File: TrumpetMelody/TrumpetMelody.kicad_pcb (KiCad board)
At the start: 2 copper layers, 76.2 x 68.6 mm, 79 parts, among them J1 USB_B_Micro, J2 Conn_01x05, J3 640456-3, J4 640456-3, SW1 SW_Push, U1 STM32F411RETx, U2 TLV62565DBVR, U3 MAX98357AETE_T, U4 MAX7375AXR805

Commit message: Placed vias so we can connect USB_ID and USB_VSENSE later if needed
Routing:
- net USB_VSENSE: track 2.18 -> 28.8 mm
- net USB_ID: track 2.79 -> 27.1 mm
- net USB_ID_Connector: track 0.00 -> 8.79 mm, vias 0 -> 1
- net +5V: vias 2 -> 3
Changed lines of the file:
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@@
   (segment (start 200.677011 73.914) (end 200.677011 76.379567) (width 0.254) (layer "F.Cu") (net 5))
   (segment (start 200.677011 76.379567) (end 200.635527 76.421051) (width 0.254) (layer "F.Cu") (net 5))
+  (segment (start 154.278422 93.293422) (end 154.278422 92.736578) (width 0.61) (layer "F.Cu") (net 6))
   (segment (start 192.065 105.41) (end 193.105 104.37) (width 0.61) (layer "F.Cu") (net 6))
   (segment (start 154.278422 97.872954) (end 153.280224 96.874756) (width 0.61) (layer "F.Cu") (net 6))
@@
   (segment (start 160.067 85.01) (end 160.147 85.09) (width 0.61) (layer "F.Cu") (net 6))
   (segment (start 193.105 102.935) (end 193.04 102.87) (width 0.61) (layer "F.Cu") (net 6))
+  (segment (start 154.355 93.37) (end 154.278422 93.293422) (width 0.61) (layer "F.Cu") (net 6))
   (segment (start 193.105 104.37) (end 193.105 102.935) (width 0.61) (layer "F.Cu") (net 6))
   (segment (start 192.45 105.025) (end 197.32 105.025) (width 0.2) (layer "F.Cu") (net 6))
-  (segment (start 154.278422 97.872954) (end 154.278422 92.736578) (width 0.61) (layer "F.Cu") (net 6))
+  (segment (start 154.278422 93.446578) (end 154.355 93.37) (width 0.61) (layer "F.Cu") (net 6))
+  (segment (start 154.278422 97.872954) (end 154.278422 93.446578) (width 0.61) (layer "F.Cu") (net 6))
   (segment (start 150.105 100.782195) (end 161.186659 111.863854) (width 0.61) (layer "F.Cu") (net 6))
   (segment (start 197.32 105.525) (end 192.18 105.525) (width 0.2) (layer "F.Cu") (net 6))
@@
   (via (at 160.147 85.09) (size 0.6) (drill 0.3) (layers "F.Cu" "B.Cu") (net 6))
   (via (at 155.321 89.408) (size 0.6) (drill 0.3) (layers "F.Cu" "B.Cu") (net 6))
+  (via (at 154.355 93.37) (size 0.6) (drill 0.3) (layers "F.Cu" "B.Cu") (net 6))
   (segment (start 155.321 85.09) (end 155.321 89.408) (width 0.61) (layer "B.Cu") (net 6))
   (segment (start 160.147 85.09) (end 155.321 85.09) (width 0.61) (layer "B.Cu") (net 6))
@@
   (segment (start 154.278422 99.472954) (end 159.385 104.579532) (width 0.254) (layer "F.Cu") (net 28))
   (segment (start 159.385 104.888769) (end 160.605925 106.109694) (width 0.254) (layer "F.Cu") (net 28))
+  (via (at 158.605 101.37) (size 0.6) (drill 0.3) (layers "F.Cu" "B.Cu") (net 29))
+  (segment (start 153.078422 100.272954) (end 153.078422 102.593422) (width 0.254) (layer "B.Cu") (net 29))
+  (segment (start 153.078422 102.593422) (end 153.605 103.12) (width 0.254) (layer "B.Cu") (net 29))
+  (segment (start 153.605 103.12) (end 156.855 103.12) (width 0.254) (layer "B.Cu") (net 29))
+  (segment (start 156.855 103.12) (end 158.605 101.37) (width 0.254) (layer "B.Cu") (net 29))
   (segment (start 178.489977 102.87) (end 186.055 102.87) (width 0.254) (layer "F.Cu") (net 30))
   (segment (start 186.055 102.87) (end 187.96 100.965) (width 0.254) (layer "F.Cu") (net 30))
@@
   (segment (start 208.28 97.155) (end 208.28 68.151) (width 0.254) (layer "B.Cu") (net 69))
   (segment (start 204.47 100.965) (end 208.28 97.155) (width 0.254) (layer "B.Cu") (net 69))
-  (segment (start 180.092369 89.418758) (end 181.603482 87.907644) (width 0.254) (layer "F.Cu") (net 78))
-  (segment (start 180.092369 89.461897) (end 180.092369 89.418758) (width 0.254) (layer "F.Cu") (net 78))
-  (via (at 180.092369 89.461897) (size 0.6) (drill 0.381) (layers "F.Cu" "B.Cu") (free) (net 78))
-  (segment (start 180.276607 90.164371) (end 180.719369 89.721609) (width 0.254) (layer "F.Cu") (net 79))
+  (segment (start 156.838 94.353) (end 162.438712 94.353) (width 0.254) (layer "F.Cu") (net 78))
+  (segment (start 155.855 93.37) (end 156.838 94.353) (width 0.254) (layer "F.Cu") (net 78))
+  (segment (start 163.421712 93.37) (end 176.141126 93.37) (width 0.254) (layer "F.Cu") (net 78))
+  (segment (start 162.438712 94.353) (end 163.421712 93.37) (width 0.254) (layer "F.Cu") (net 78))
+  (segment (start 176.141126 93.37) (end 181.603482 87.907644) (width 0.254) (layer "F.Cu") (net 78))
+  (via (at 155.855 93.37) (size 0.6) (drill 0.381) (layers "F.Cu" "B.Cu") (free) (net 78))
   (segment (start 180.719369 89.498865) (end 181.957035 88.261198) (width 0.254) (layer "F.Cu") (net 79))
+  (segment (start 176.087978 94.353) (end 180.719369 89.721609) (width 0.254) (layer "F.Cu") (net 79))
+  (segment (start 159.855 100.12) (end 165.622 94.353) (width 0.254) (layer "F.Cu") (net 79))
+  (segment (start 165.622 94.353) (end 176.087978 94.353) (width 0.254) (layer "F.Cu") (net 79))
   (segment (start 180.719369 89.721609) (end 180.719369 89.498865) (width 0.254) (layer "F.Cu") (net 79))
-  (segment (start 180.083002 90.164371) (end 180.276607 90.164371) (width 0.254) (layer "F.Cu") (net 79))
-  (via (at 180.083002 90.164371) (size 0.6) (drill 0.381) (layers "F.Cu" "B.Cu") (free) (net 79))
+  (via (at 159.855 100.12) (size 0.6) (drill 0.381) (layers "F.Cu" "B.Cu") (free) (net 79))
   (zone (net 38) (net_name "Net-(U2-SW)") (layer "F.Cu") (hatch edge 0.5)
     (priority 1)

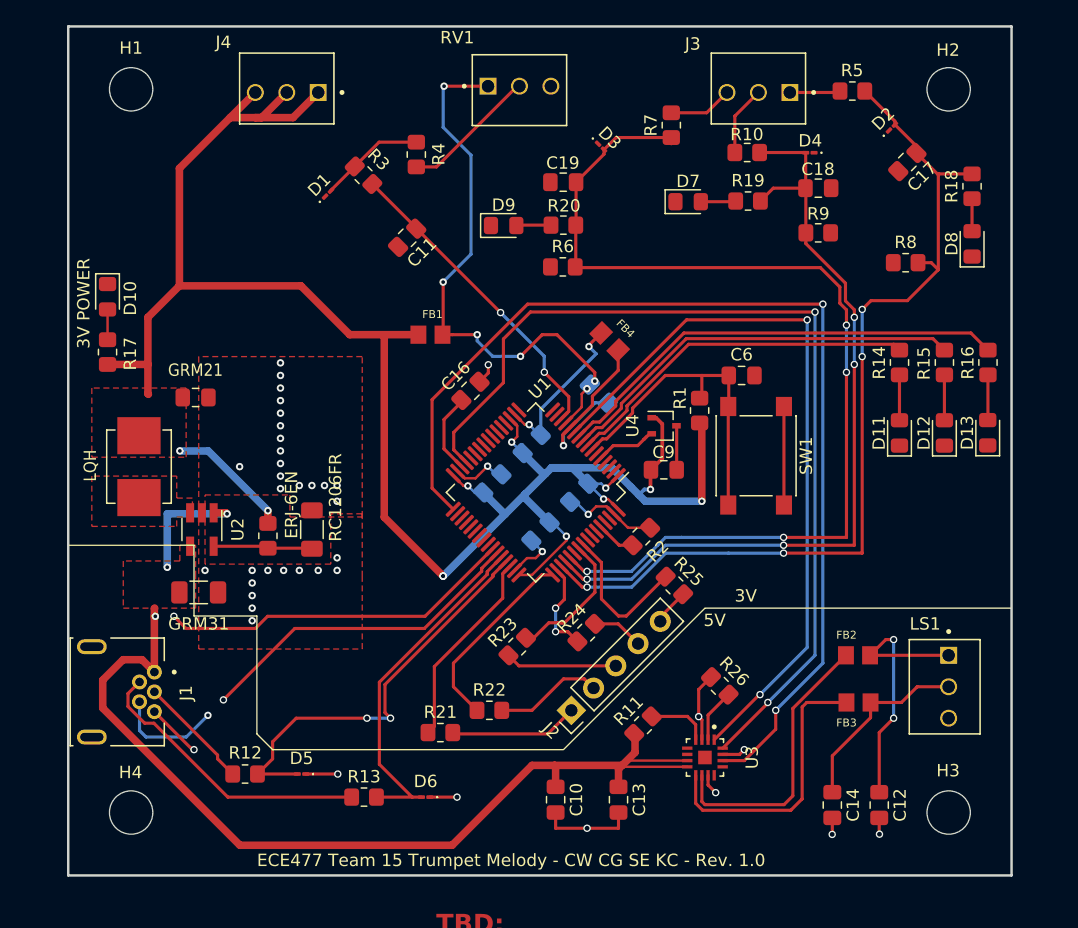
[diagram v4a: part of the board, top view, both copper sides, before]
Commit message: Initialized GND Planes and tweaked stitching vias
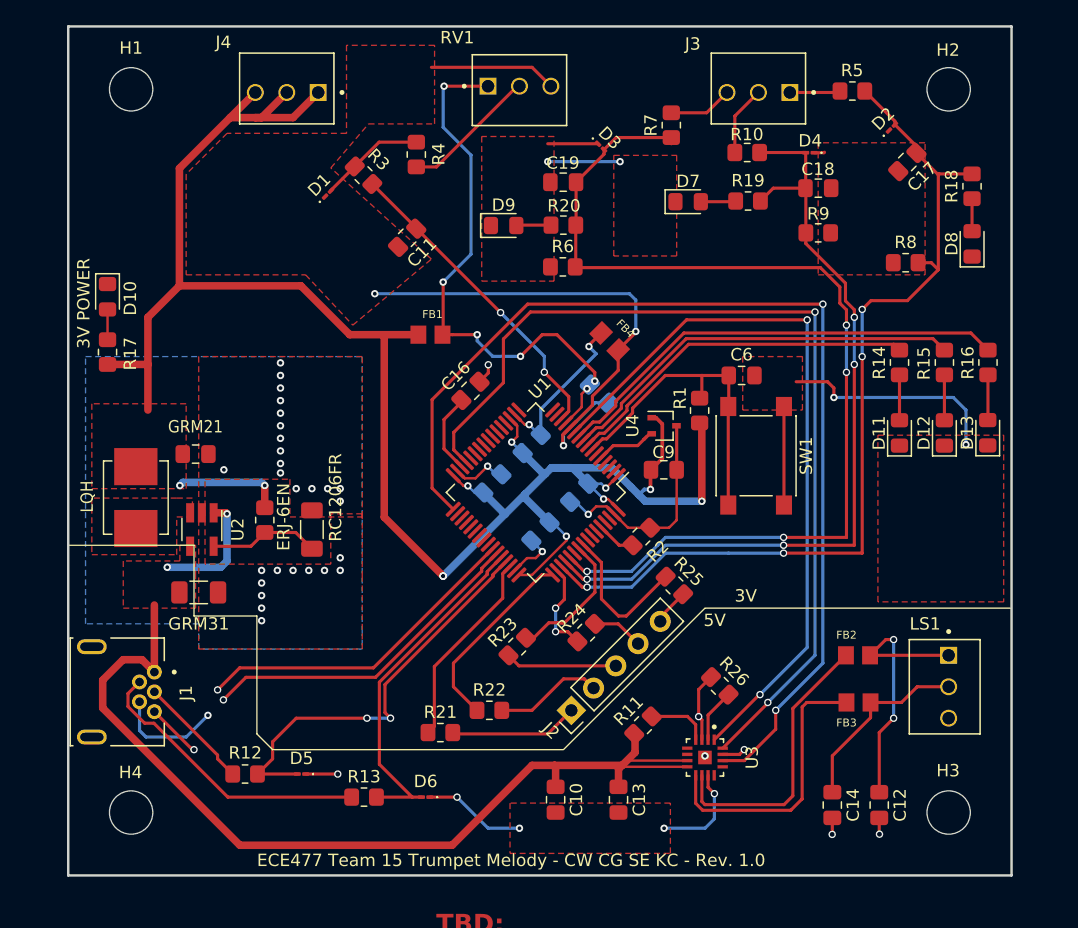
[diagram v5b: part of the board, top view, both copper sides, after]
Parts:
- moved GRM21 4.57 mm to (157.6, 80.3)
- moved LQH 2.51 mm to (152.8, 83.8)
- moved ERJ-6EN 1.30 mm to (163.2, 85.6)
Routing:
- net GND: track 69.2 -> 109.2 mm, vias 13 -> 45
- net GNDA: track 17.8 -> 54.0 mm, vias 3 -> 5
- net USB_VSENSE: track 28.8 -> 26.9 mm
- net Net-(U2-FB): track 8.02 -> 8.94 mm
- net +5V: track 89.0 -> 88.9 mm, vias 3 -> 2
- net PadMax: vias 0 -> 1
- net (no net): vias 29 -> 0
- added copper zone on B.Cu, net GND
- added copper zone on F.Cu, net GNDA

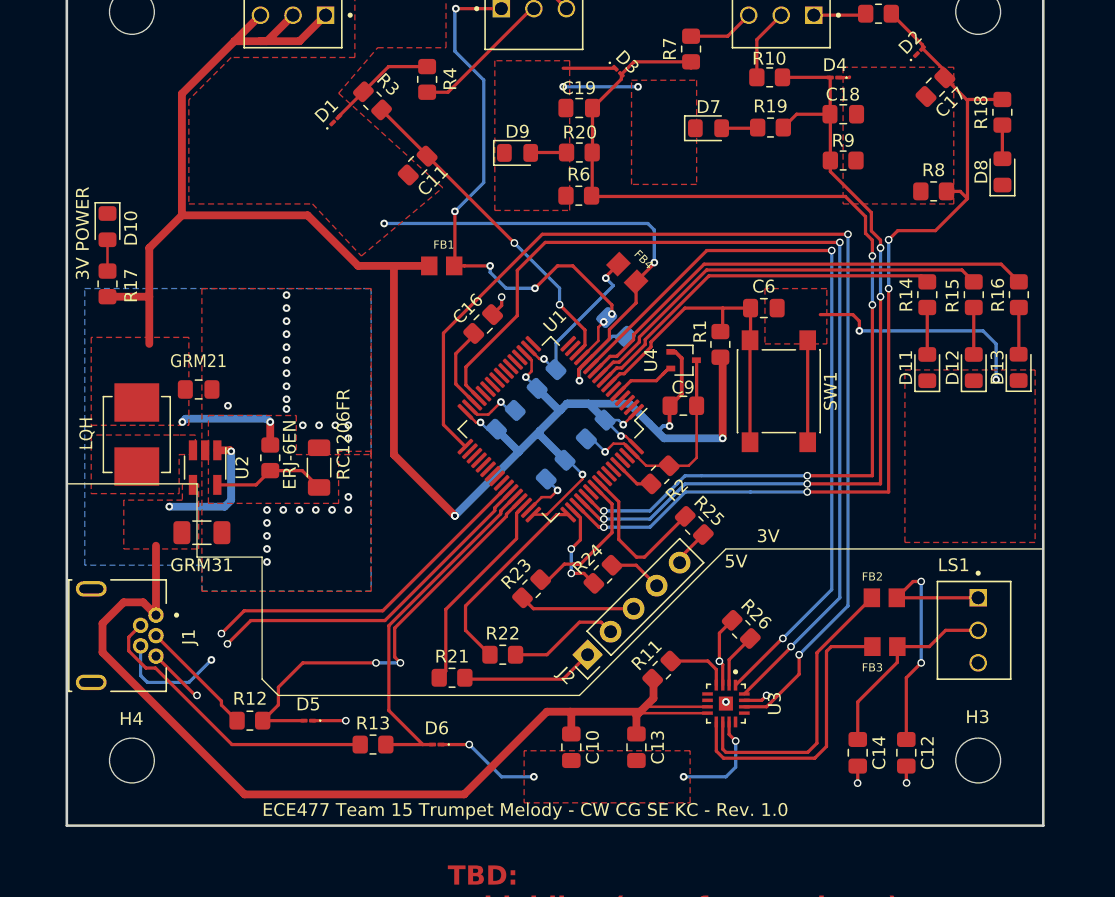
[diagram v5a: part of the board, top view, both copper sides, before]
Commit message: public enemy #1: analog ground
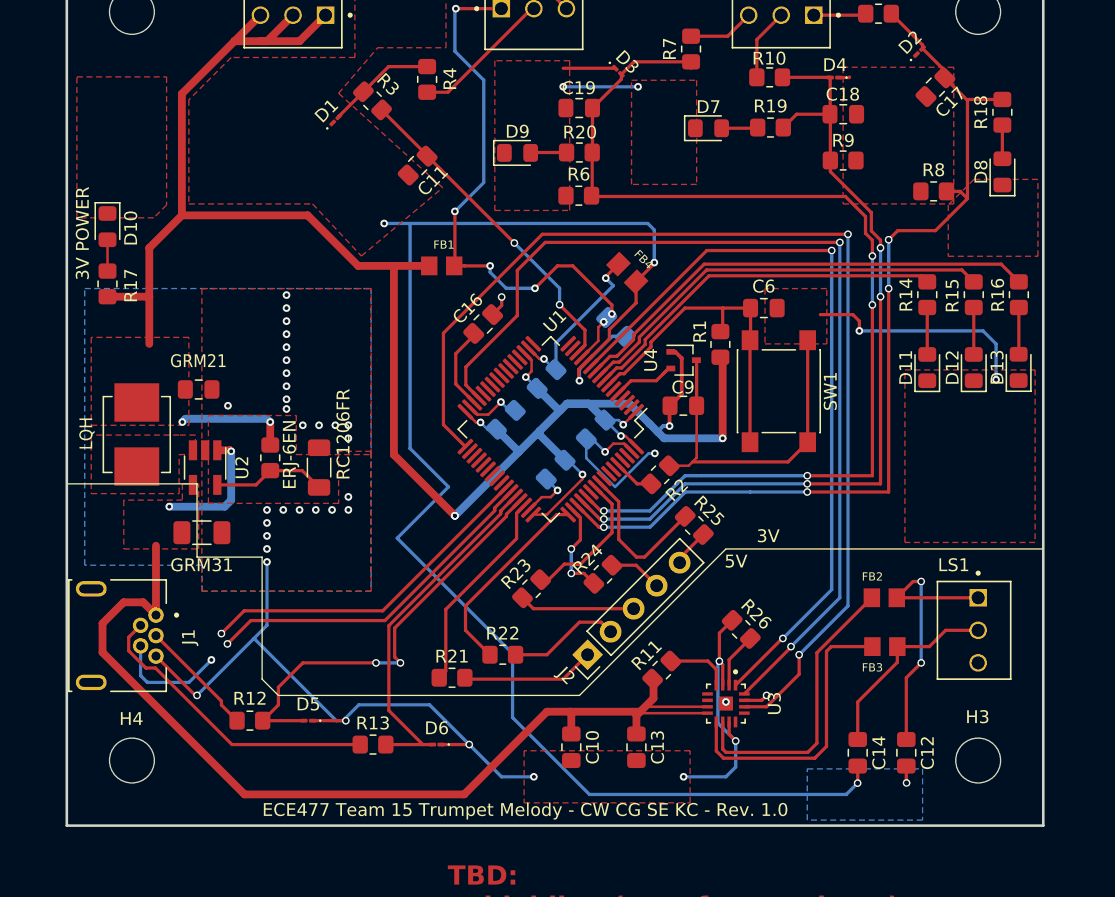
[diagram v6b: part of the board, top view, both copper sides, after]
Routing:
- net GNDA: track 54.0 -> 129.0 mm
- net GND: track 109.2 -> 165.2 mm, vias 45 -> 46
- added copper zone on B.Cu, net GNDA

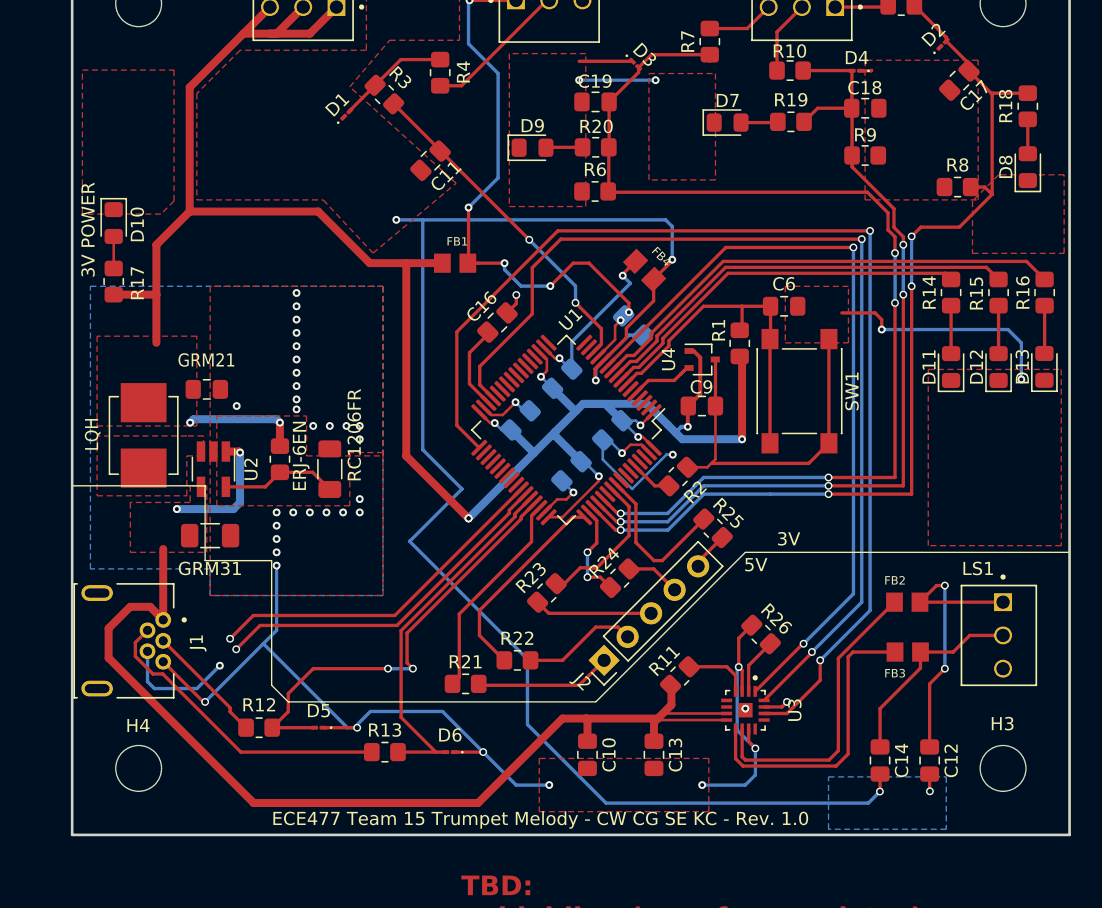
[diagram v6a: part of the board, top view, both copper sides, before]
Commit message: Added FB to simplify AGND
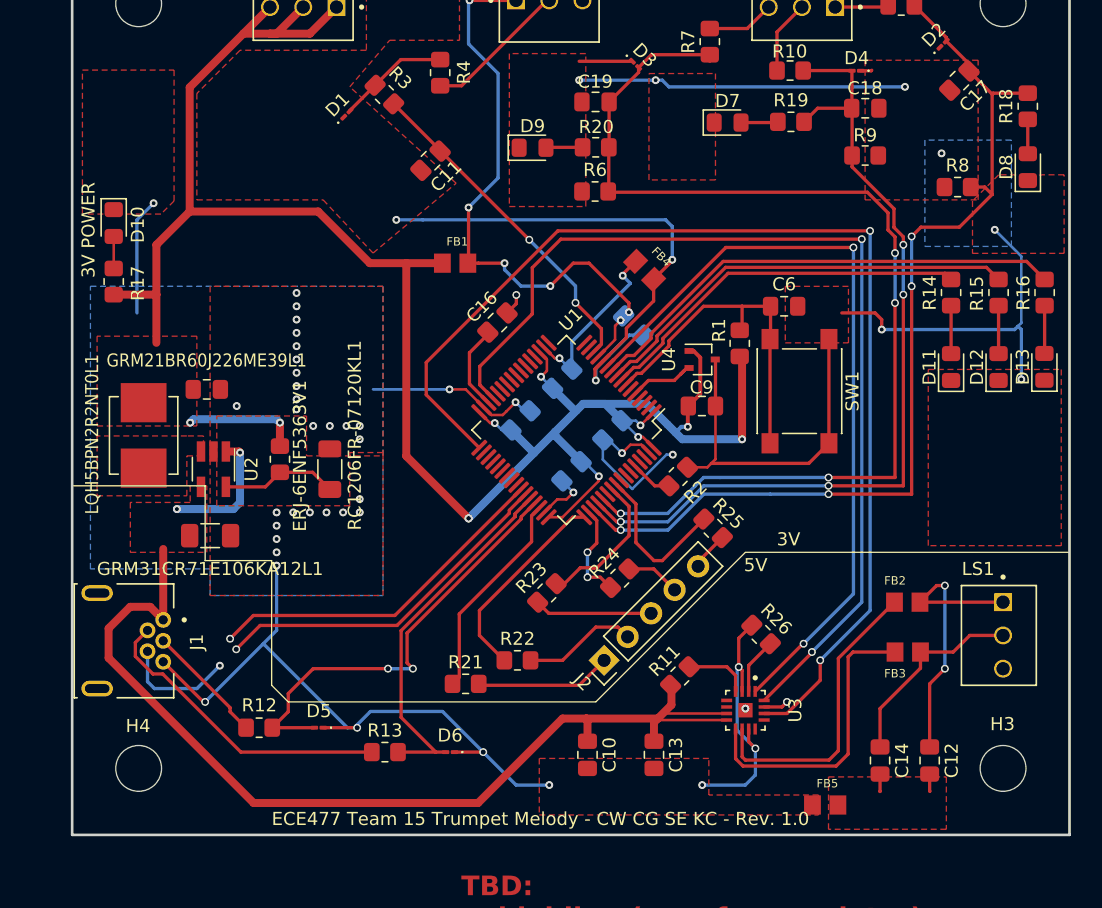
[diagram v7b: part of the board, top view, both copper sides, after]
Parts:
- added FB5: FerriteBead, TrumpetMelodyFootprintLibrary:FB_LI0805G201R-10, F.Cu at (204.9, 112.0)
- renumbered ERJ-6EN to ERJ-6ENF5363V1, GRM21 to GRM21BR60J226ME39L1, GRM31 to GRM31CR71E106KA12L1, LQH to LQH5BPN2R2NT0L1, RC1206FR to RC1206FR-07120KL1
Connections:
- C12 pad 2: GNDA -> Net-(C12-Pad2)
- C14 pad 2: GNDA -> Net-(C12-Pad2)
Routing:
- net GNDA: track 129.0 -> 51.4 mm, vias 5 -> 3
- net GND: track 165.2 -> 211.5 mm, vias 46 -> 51
- net Net-(C12-Pad2): track 0.00 -> 2.66 mm
- net I2S_WS: track 85.6 -> 87.5 mm
- added copper zone on F.Cu, net Net-(C12-Pad2)
- removed copper zone on B.Cu, net GNDA
